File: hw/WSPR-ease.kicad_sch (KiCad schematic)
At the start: 46 parts, among them J101 pwr+data, J102 SMA, J103 SMA, Q101 IRLML2060, U101 SRV05-4, U102 ESP32-S3-WROOM-1-N8R8, U103 LMR51430YDDCR, U104 GNSS module

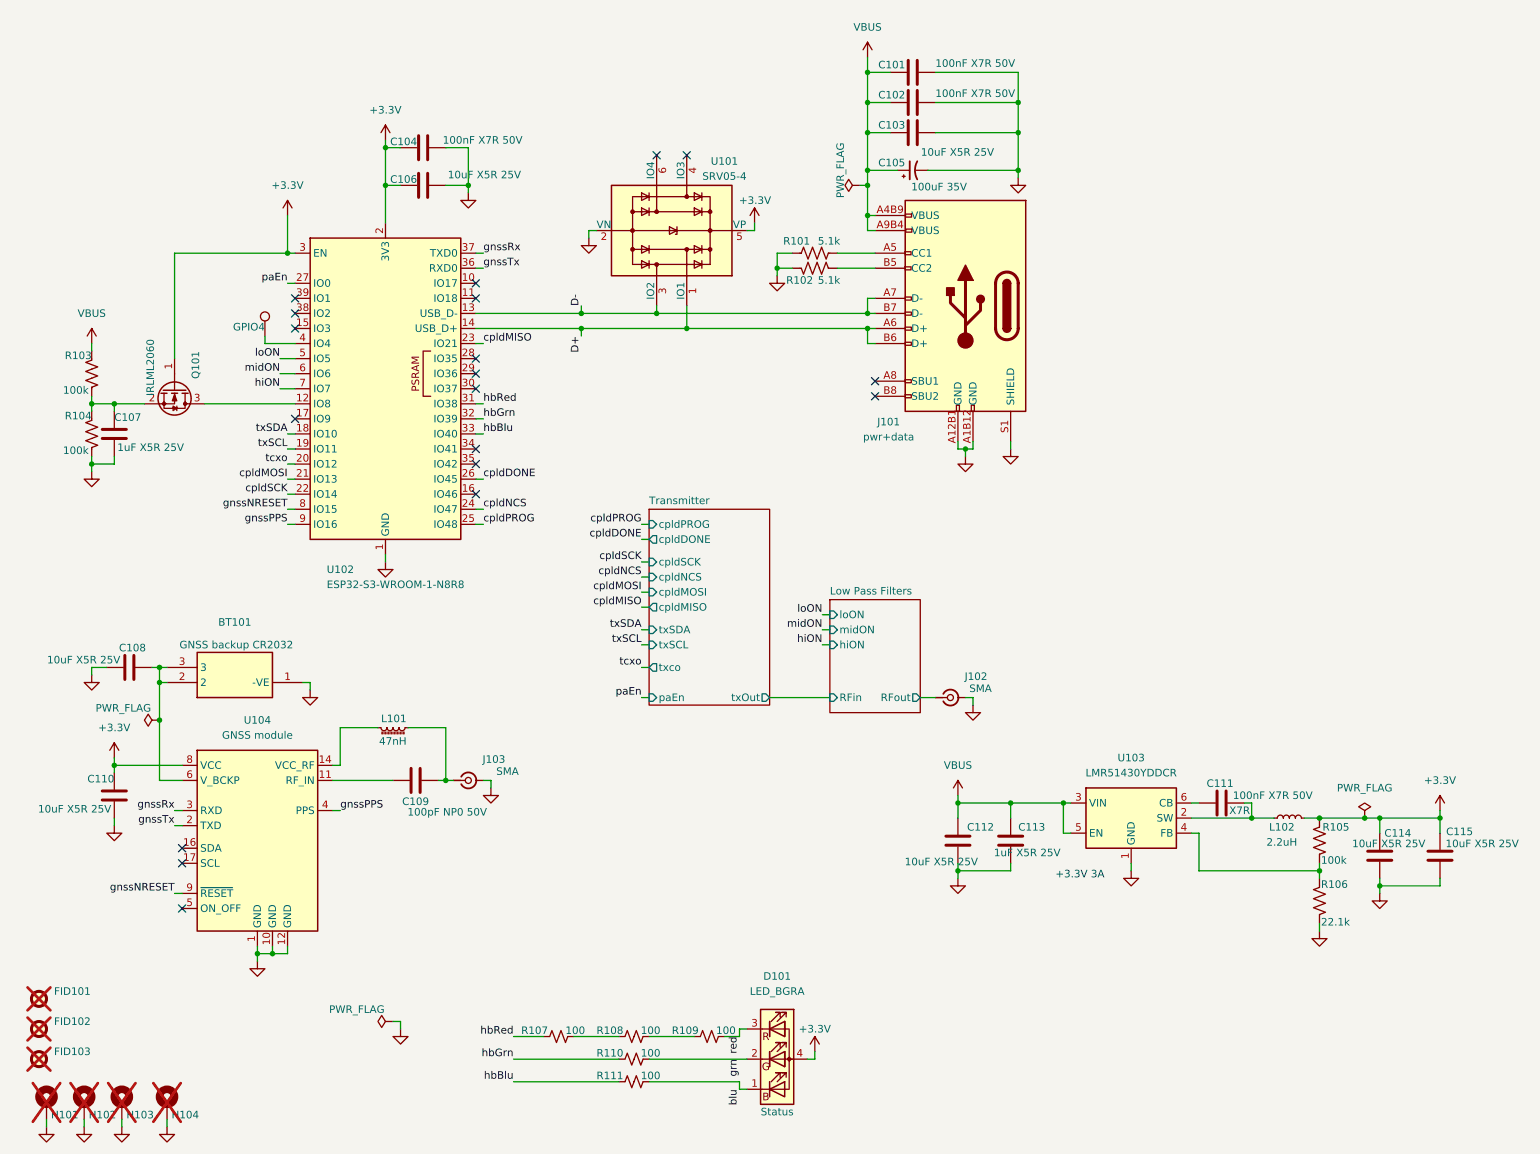
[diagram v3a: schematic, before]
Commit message: Prep to go back to FPGA. Board is routed except for power layer zones. No time to run DRC yet.
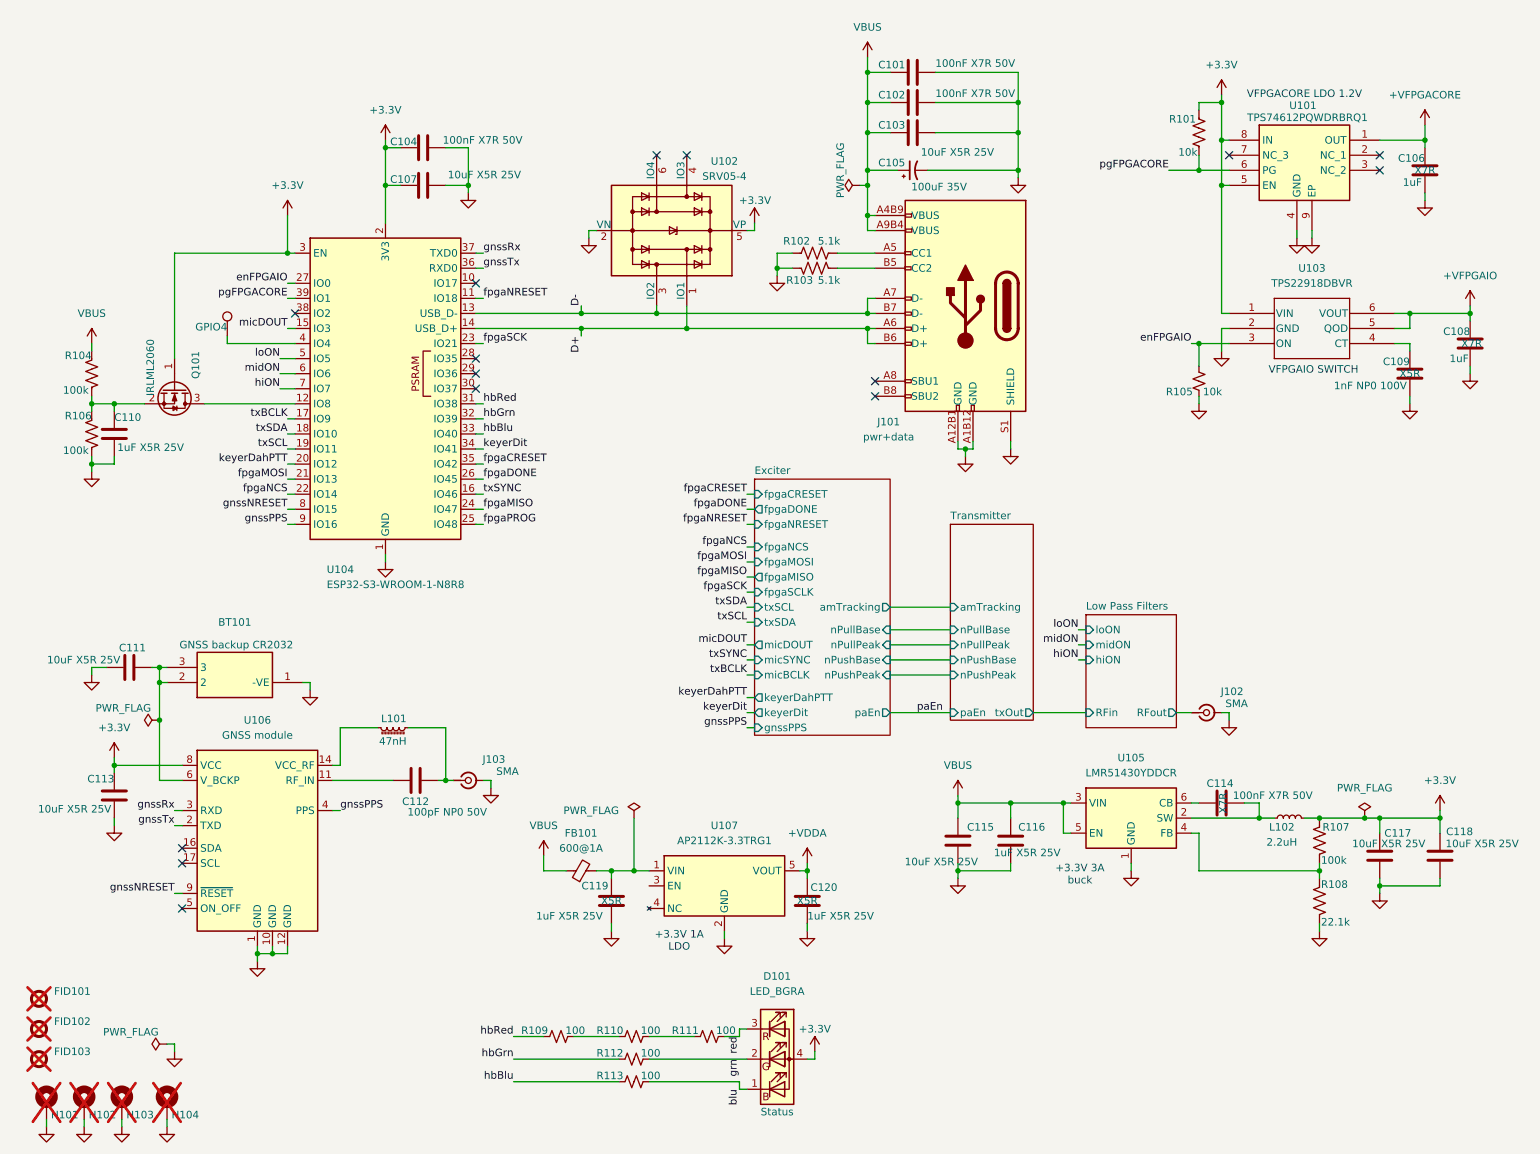
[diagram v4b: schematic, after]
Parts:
- added C106, C108: 1uF, Capacitor_SMD:C_0402_1005Metric, symbol Device:C
- added C109: 1nF NP0 100V, Capacitor_SMD:C_0603_1608Metric, symbol Device:C
- added C119, C120: 1uF X5R 25V, Capacitor_SMD:C_0402_1005Metric, symbol Device:C
- added FB101: 600@1A, Inductor_SMD:L_0603_1608Metric, symbol Device:FerriteBead_Small
- added R101: 10k, Resistor_SMD:R_0402_1005Metric, symbol Device:R_US
- added R105: 10k, Resistor_SMD:R_0402_1005Metric, symbol Device:R_Small_US
- added U101: TPS74612PQWDRBRQ1, Library:SON65P300X300X100-9N-D, symbol Library:TPS74612PQWDRBRQ1
- added U103: TPS22918DBVR, Library:DBV6_TEX, symbol Library:TPS22918DBVR
- added U107: AP2112K-3.3TRG1, Library:SOT95P285X140-5N, symbol Library:AP2112K-3.3TRG1
- renumbered C106 to C107, C107 to C110, C108 to C111, C109 to C112, C110 to C113, C111 to C114, C112 to C115, C113 to C116, C114 to C117, C115 to C118, R101 to R102, R102 to R103, R103 to R104, R104 to R106, R105 to R107, R106 to R108, R107 to R109, R108 to R110, R109 to R111, R110 to R112, R111 to R113, U101 to U102, U102 to U104, U103 to U105, U104 to U106
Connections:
- net +3.3V: now also R101.2, U101.5 (EN), U101.8 (IN), U103.1 (VIN)
- net GND: now also C106.2, C108.2, C109.2, C119.2, C120.2, R105.1, U101.4 (GND), U101.9 (EP), U103.2 (GND), U107.2 (GND)
- net VBUS: now also FB101.1
- net paEn: no longer U104.27 (IO0)
- net fpgaNRESET: now reaches U104.11 (IO18)
- net micDOUT: now reaches U104.15 (IO3)
- net txSYNC: now reaches U104.16 (IO46)
- net txBCLK: now reaches U104.17 (IO9)
- net keyerDit: now reaches U104.34 (IO41)
- net fpgaCRESET: now reaches U104.35 (IO42)
- net pgFPGACORE: now reaches U104.39 (IO1)
- net pgFPGACORE: now also R101.1, U101.6 (PG)
- net cpldDONE renamed fpgaDONE
- net cpldMISO renamed fpgaSCK
- net cpldMOSI renamed fpgaMOSI
- net cpldNCS renamed fpgaMISO
- net cpldPROG renamed fpgaPROG
- net cpldSCK renamed fpgaNCS
- net tcxo renamed keyerDahPTT
- new net: C119.1, FB101.2, U107.1 (VIN)
- new net: C109.1, U103.4 (CT)
- new net +VDDA: C120.1, U107.5 (VOUT)
- new net +VFPGACORE: C106.1, U101.1 (OUT)
- new net +VFPGAIO: C108.1, U103.5 (QOD), U103.6 (VOUT)
- new net enFPGAIO: R105.2, U103.3 (ON), U104.27 (IO0)
- no-connect marks 19 -> 15
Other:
- added sheet Exciter (exciter.kicad_sch)
- sheet Transmitter ports: added amTracking, nPullBase, nPullPeak, nPushBase, nPushPeak; removed cpldDONE, cpldMISO, cpldMOSI, cpldNCS, cpldPROG, cpldSCK, txSCL, txSDA, txco
- note added: "+3.3V 1A LDO"
- note added: "+3.3V 3A buck"
- note added: "VFPGACORE LDO 1.2V"
- note added: "VFPGAIO SWITCH"
- note removed: "+3.3V 3A"
- moved on the sheet: J102

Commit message: Now we pass schematic and PCB DRC and 3D renders nicely also.
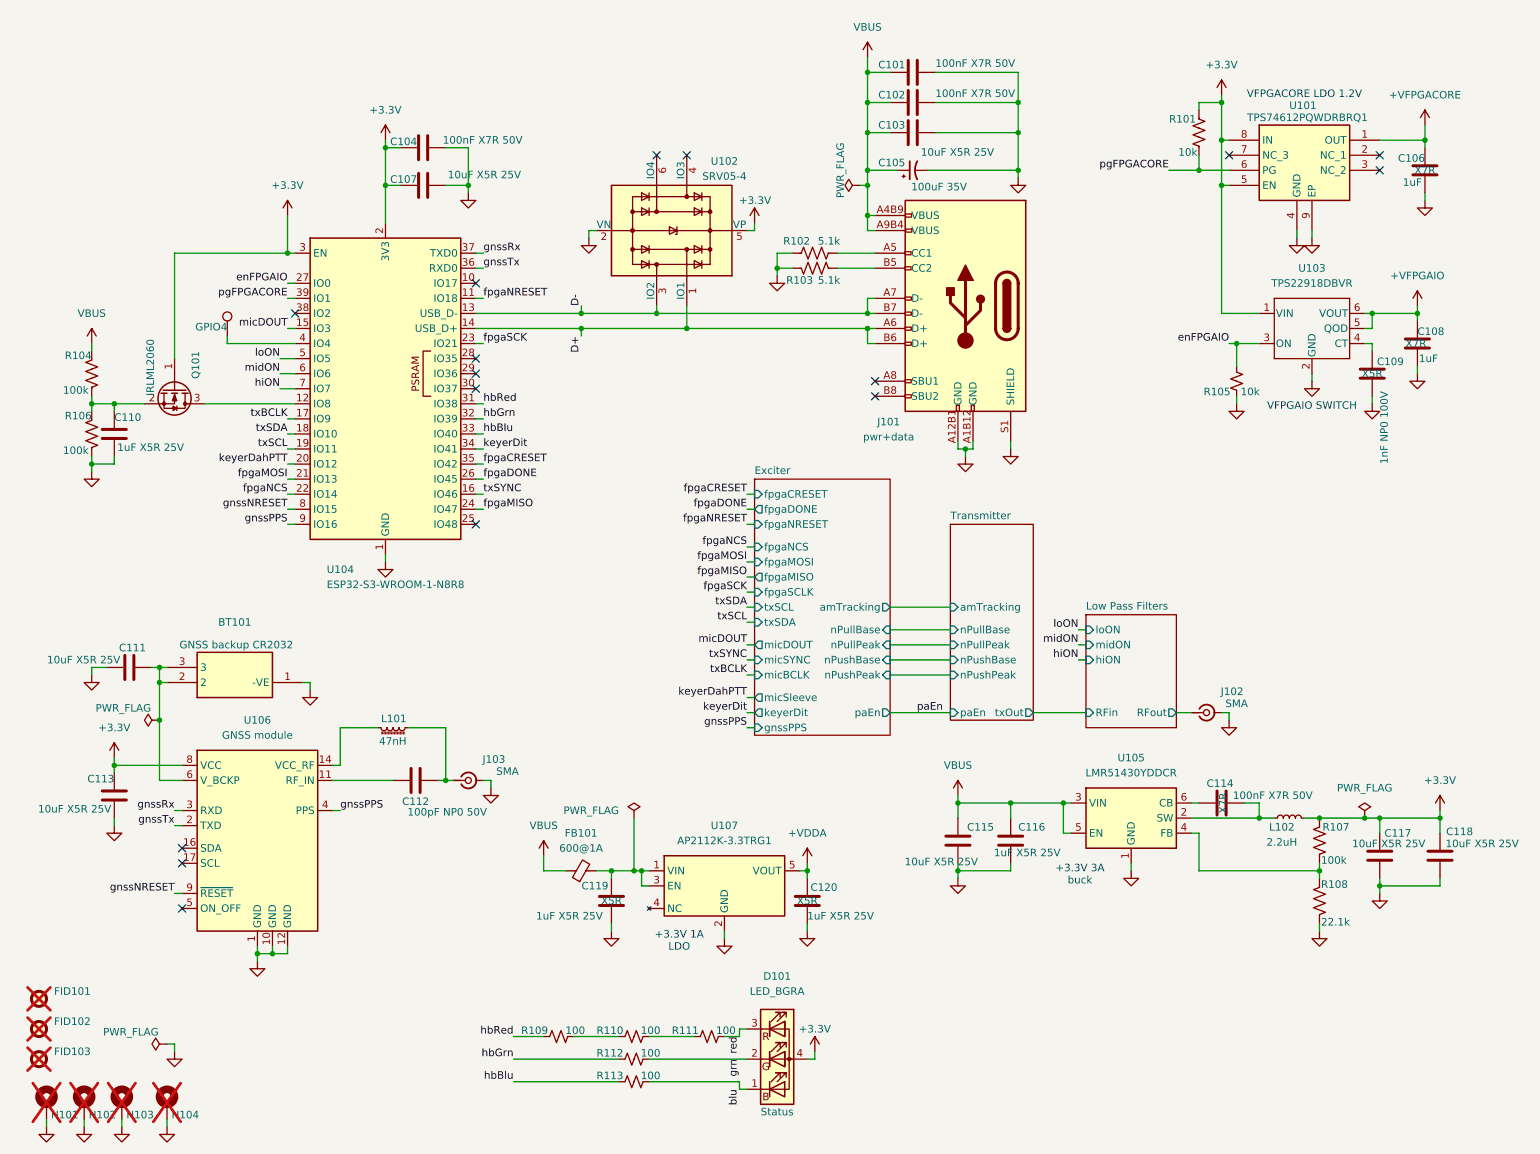
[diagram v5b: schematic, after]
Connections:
- net at C119.1, FB101.2, U107.1 (VIN): now also U107.3 (EN)
- net fpgaPROG: no longer names the net of U104.25 (IO48)
- no-connect marks 15 -> 16
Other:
- sheet Exciter ports: added micSleeve; removed keyerDahPTT
- moved on the sheet: C108, C109, R105, U103

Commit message: Remove old stuff, describe new FPGA strategy, clean up schematic to show this more cleanly, add I2S I/O for ESP32 to FPGA and mic ADC with common clocking.
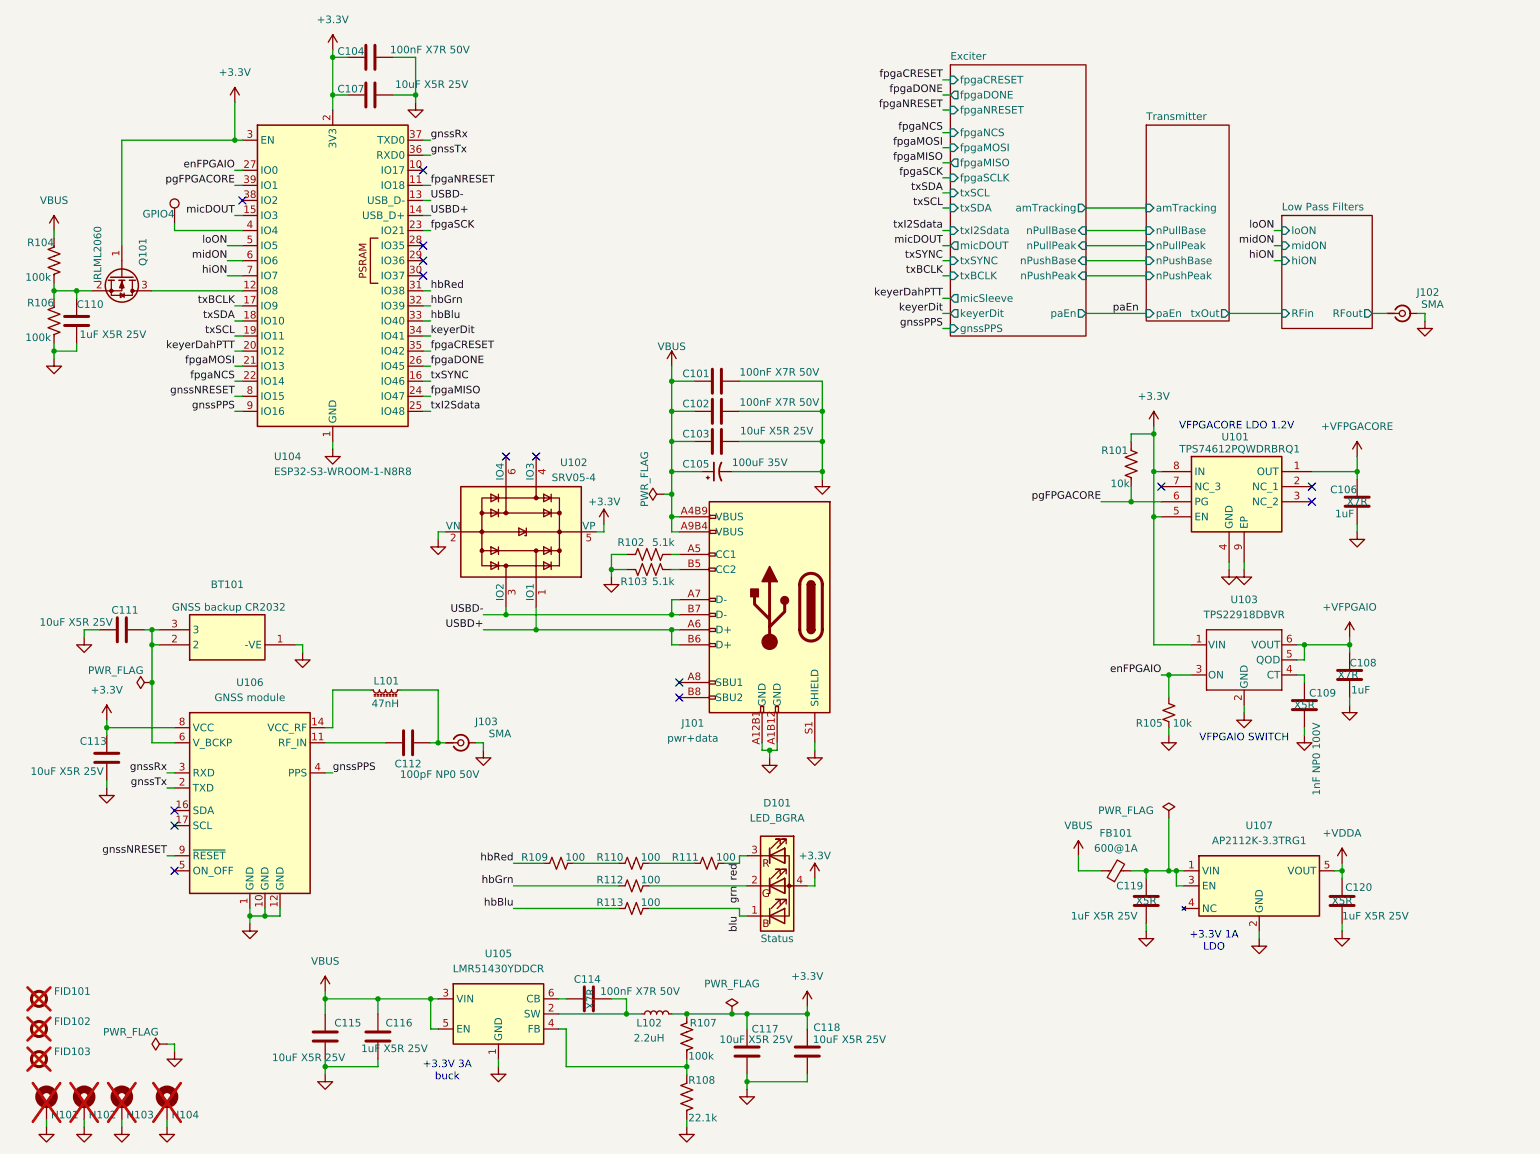
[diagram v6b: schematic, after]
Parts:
- U106: LCSC C2970256 -> C5117921; LCSCMFG (none) -> Zhongkewei; LCSCMPN (none) -> ATGM336H-5NR32
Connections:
- net txI2Sdata: now reaches U104.25 (IO48)
- net D+ renamed USBD+
- net D- renamed USBD-
- no-connect marks 16 -> 15
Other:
- sheet Exciter ports: added txBCLK, txI2Sdata, txSYNC; removed micBCLK, micSYNC
- moved on the sheet: BT101, C101, C102, C103, C104, C105, C106, C107, C108, C109, C110, C111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

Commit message: Clean up old garbage files
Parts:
- renumbered C104 to C101, C107 to C102, C110 to C103, C101 to C104, C102 to C105, C103 to C106, C105 to C107, C106 to C109, C109 to C110, C119 to C114, C120 to C115, C114 to C116, C115 to C117, C116 to C118, C117 to C119, C118 to C120, J102 to J101, J101 to J102, R104 to R101, R106 to R102, R102 to R103, R103 to R104, R101 to R105, R105 to R106, R109 to R107, R110 to R108, R111 to R109, R112 to R110, R113 to R111, R107 to R112, R108 to R113, U104 to U101, U101 to U104, U106 to U105, U107 to U106, U105 to U107
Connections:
- net txBCLK renamed modBCLK
- net txI2Sdata renamed modTxData
- net txSYNC renamed modSYNC
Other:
- sheet Exciter ports: added fpgaSCK, modBCLK, modSYNC, modTxData; removed fpgaSCLK, txBCLK, txI2Sdata, txSYNC
- moved on the sheet: C108, C109, C110, C114, C115, FB101, R105, R106, U103, U104, U106
